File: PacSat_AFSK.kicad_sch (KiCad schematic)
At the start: 4 parts

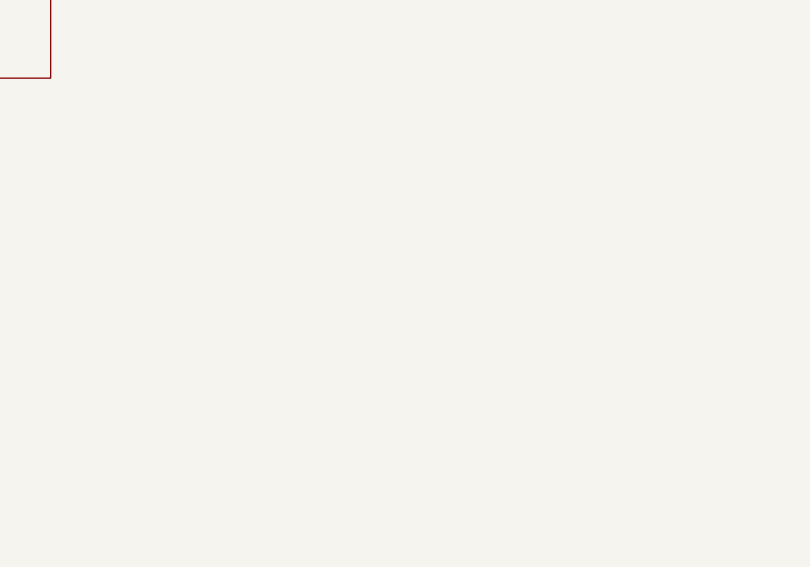
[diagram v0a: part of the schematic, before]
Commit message: Add active/standby configuration for the board
Signed-off-by: Corey Minyard <corey@minyard.net>
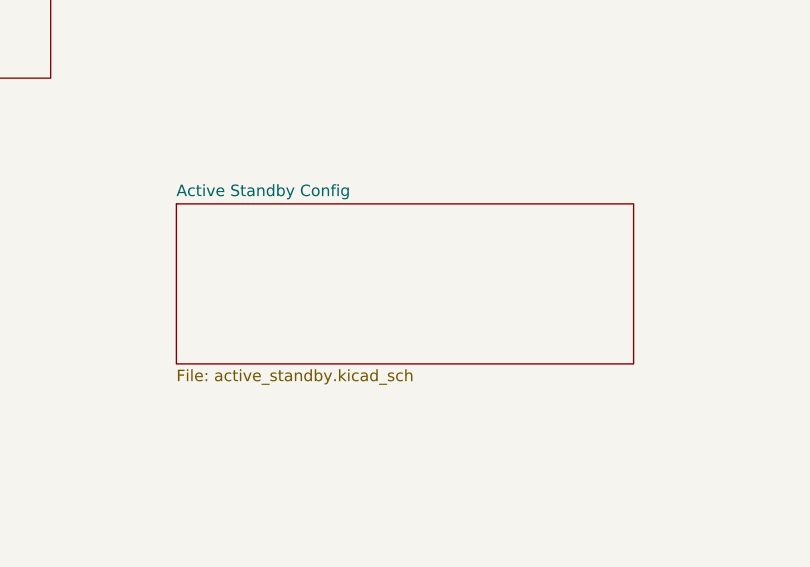
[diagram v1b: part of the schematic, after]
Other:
- added sheet Active Standby Config (active_standby.kicad_sch)
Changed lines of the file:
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@@
+	)
+	(sheet
+		(at 113.03 127)
+		(size 50.8 17.78)
+		(exclude_from_sim no)
+		(in_bom yes)
+		(on_board yes)
+		(dnp no)
+		(fields_autoplaced yes)
+		(stroke
+			(width 0.1524)
+			(type solid)
+		)
+		(fill
+			(color 0 0 0 0.0000)
+		)
+		(property "Sheetname" "Active Standby Config"
+			(at 113.03 126.2884 0)
+			(effects
+				(font
+					(size 1.27 1.27)
+				)
+				(justify left bottom)
+			)
+		)
+		(property "Sheetfile" "active_standby.kicad_sch"
+			(at 113.03 145.3646 0)
+			(effects
+				(font
+					(size 1.27 1.27)
+				)
+				(justify left top)
+			)
+		)
+		(instances
+			(project "PacSat_AFSK"
+				(path "/cc9f42d2-6985-41ac-acab-5ab7b01c5b38"
+					(page "15")
+				)
+			)
+		)
 	)
 	(sheet

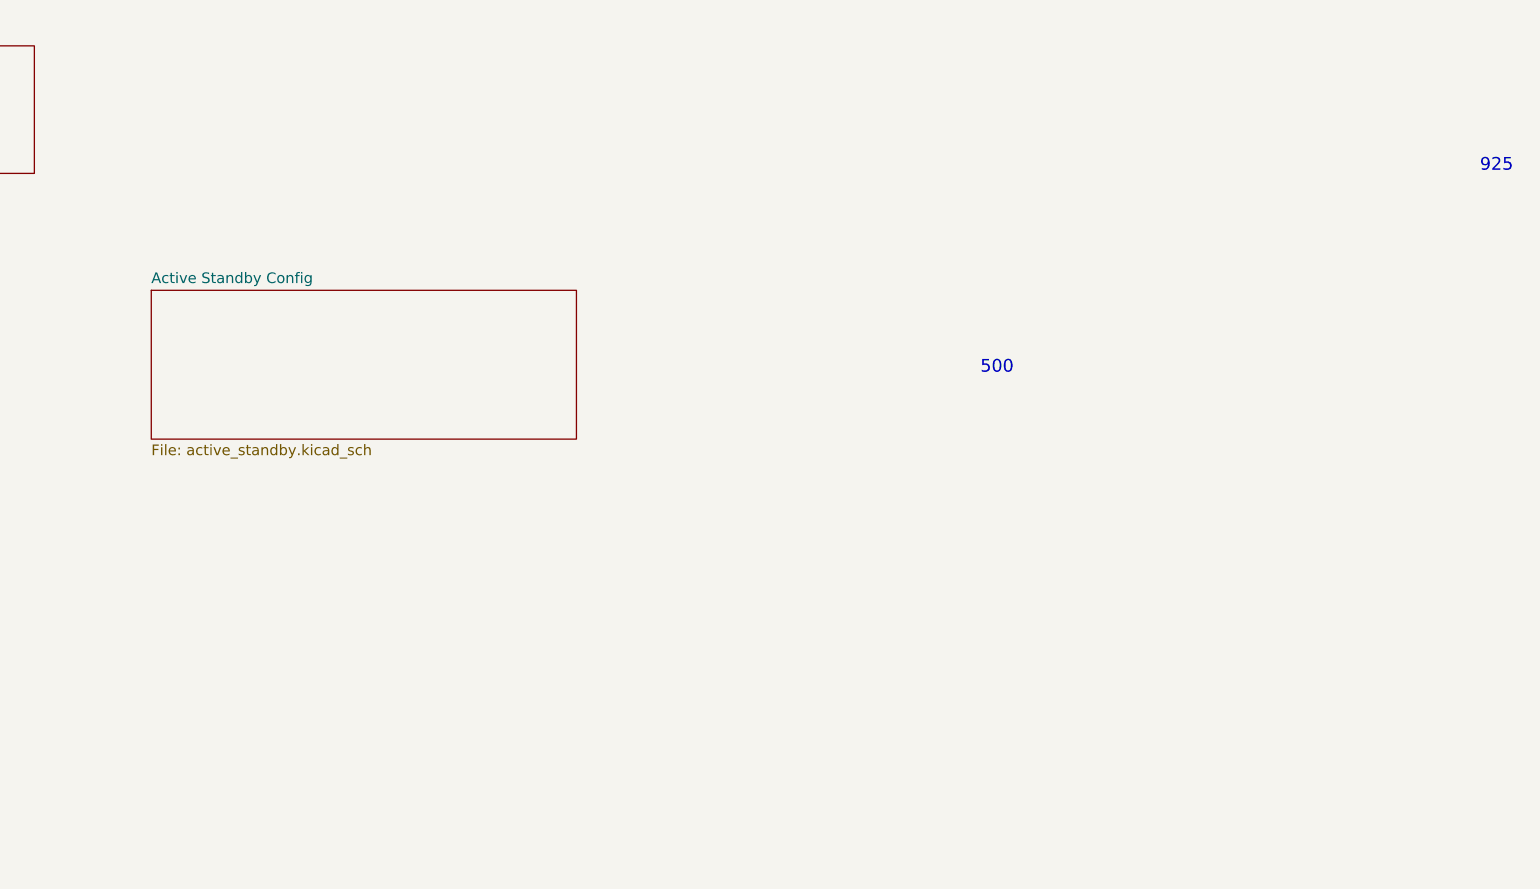
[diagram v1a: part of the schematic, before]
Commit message: Added active/standy support for TX RF and did docs
Signed-off-by: Corey Minyard <corey@minyard.net>
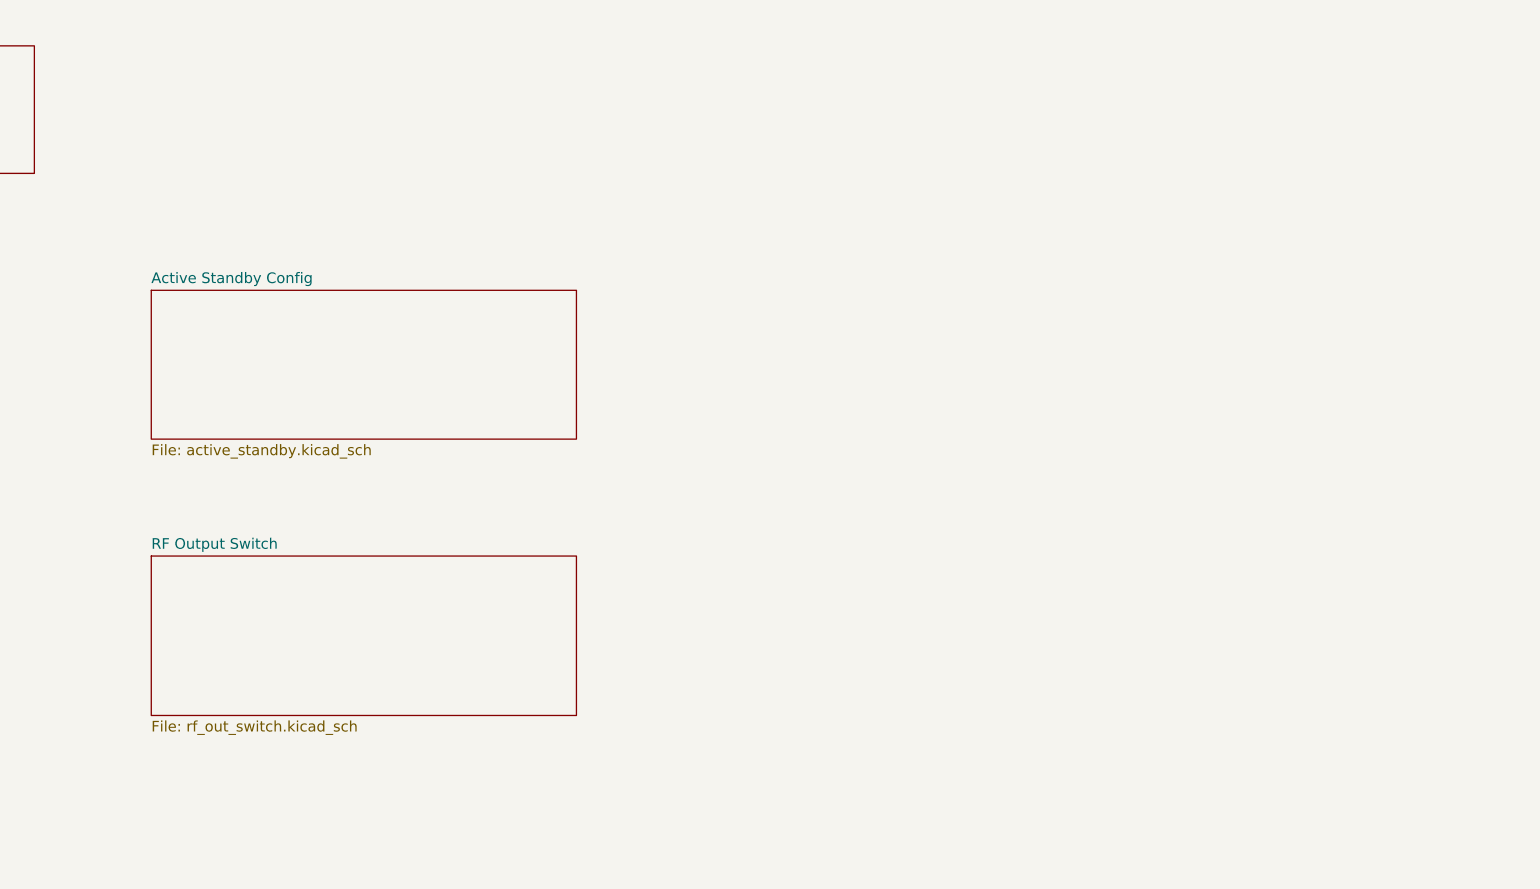
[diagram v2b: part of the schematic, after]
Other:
- added sheet RF Output Switch (rf_out_switch.kicad_sch)
- note removed: "500"
- note removed: "925"
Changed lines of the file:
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@@
 		(comment 1 "N5BRG")
-	)
-	(text "500"
-		(exclude_from_sim no)
-		(at 212.09 137.16 0)
-		(effects
-			(font
-				(size 1.524 1.524)
-			)
-			(justify left bottom)
-		)
-	)
-	(text "925"
-		(exclude_from_sim no)
-		(at 271.78 113.03 0)
-		(effects
-			(font
-				(size 1.524 1.524)
-			)
-			(justify left bottom)
-		)
 	)
 	(junction
@@
 				)
 			)
+		)
+	)
+	(sheet
+		(at 113.03 158.75)
+		(size 50.8 19.05)
+		(exclude_from_sim no)
+		(in_bom yes)
+		(on_board yes)
+		(dnp no)
+		(fields_autoplaced yes)
+		(stroke
+			(width 0.1524)
+			(type solid)
+		)
+		(fill
+			(color 0 0 0 0.0000)
+		)
+		(property "Sheetname" "RF Output Switch"
+			(at 113.03 158.0384 0)
+			(effects
+				(font
+					(size 1.27 1.27)
+				)
+				(justify left bottom)
+			)
+		)
+		(property "Sheetfile" "rf_out_switch.kicad_sch"
+			(at 113.03 178.3846 0)
+			(effects
+				(font
+					(size 1.27 1.27)
+				)
+				(justify left top)
+			)
+		)
+		(instances
+			(project "PacSat_AFSK"
+				(path "/cc9f42d2-6985-41ac-acab-5ab7b01c5b38"
+					(page "16")
+				)
+			)

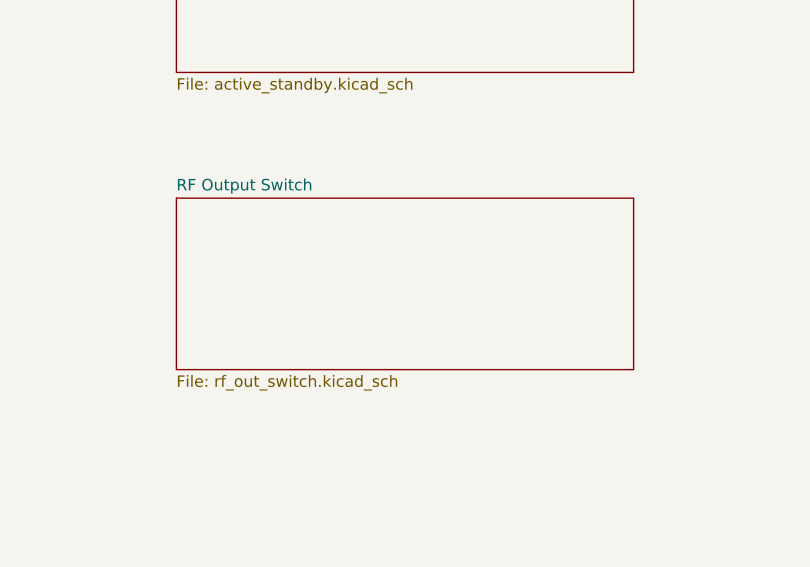
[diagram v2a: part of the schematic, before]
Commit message: Add missing sheets, move active standby to its own hierarchy
Signed-off-by: Corey Minyard <corey@minyard.net>
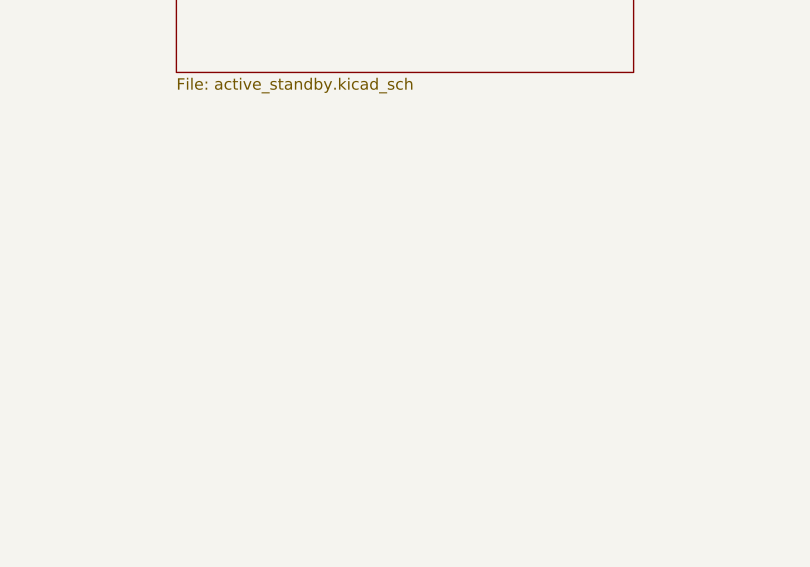
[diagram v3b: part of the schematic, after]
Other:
- removed sheet RF Output Switch
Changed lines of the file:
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@@
-	)
-	(sheet
-		(at 113.03 158.75)
-		(size 50.8 19.05)
-		(exclude_from_sim no)
-		(in_bom yes)
-		(on_board yes)
-		(dnp no)
-		(fields_autoplaced yes)
-		(stroke
-			(width 0.1524)
-			(type solid)
-		)
-		(fill
-			(color 0 0 0 0.0000)
-		)
-		(property "Sheetname" "RF Output Switch"
-			(at 113.03 158.0384 0)
-			(effects
-				(font
-					(size 1.27 1.27)
-				)
-				(justify left bottom)
-			)
-		)
-		(property "Sheetfile" "rf_out_switch.kicad_sch"
-			(at 113.03 178.3846 0)
-			(effects
-				(font
-					(size 1.27 1.27)
-				)
-				(justify left top)
-			)
-		)
-		(instances
-			(project "PacSat_AFSK"
-				(path "/cc9f42d2-6985-41ac-acab-5ab7b01c5b38"
-					(page "16")
-				)
-			)
-		)
 	)
 	(sheet

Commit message: Work on cleaning up all values for things
Signed-off-by: Corey Minyard <corey@minyard.net>
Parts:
- H2, H3, H4, H5: now left out of the parts list
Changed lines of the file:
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@@
 		(unit 1)
 		(exclude_from_sim no)
-		(in_bom yes)
+		(in_bom no)
 		(on_board yes)
 		(dnp no)
@@
 		(unit 1)
 		(exclude_from_sim no)
-		(in_bom yes)
+		(in_bom no)
 		(on_board yes)
 		(dnp no)
@@
 		(unit 1)
 		(exclude_from_sim no)
-		(in_bom yes)
+		(in_bom no)
 		(on_board yes)
 		(dnp no)
@@
 		(unit 1)
 		(exclude_from_sim no)
-		(in_bom yes)
+		(in_bom no)
 		(on_board yes)
 		(dnp no)

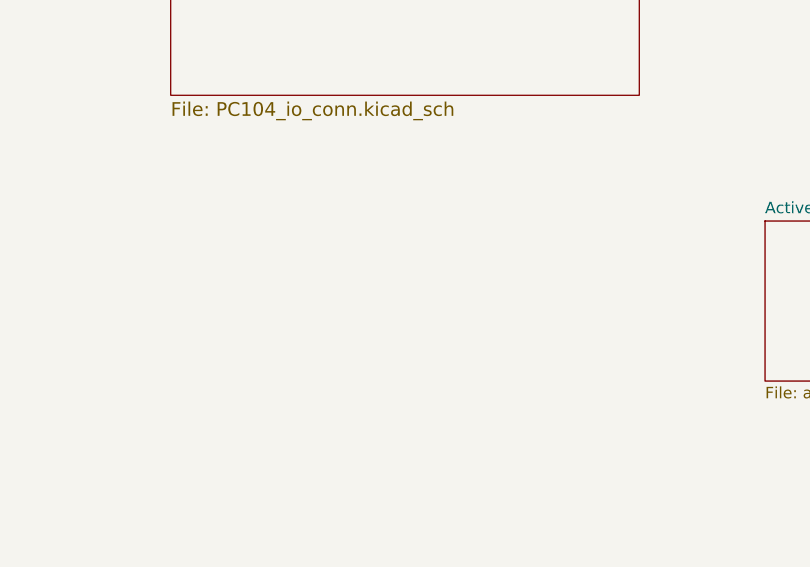
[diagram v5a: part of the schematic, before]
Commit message: Add Power System Adapter function to the board
Signed-off-by: Corey Minyard <corey@minyard.net>
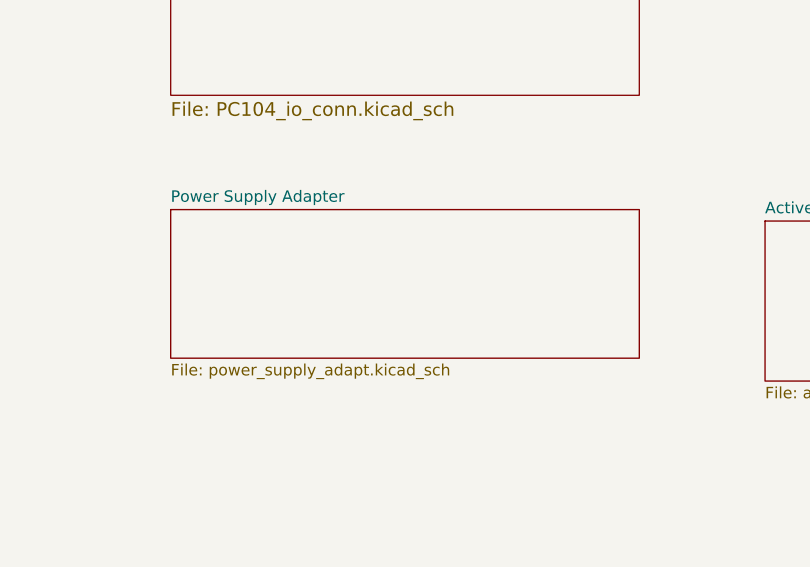
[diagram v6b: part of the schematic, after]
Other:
- added sheet Power Supply Adapter (power_supply_adapt.kicad_sch)
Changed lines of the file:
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@@
+	)
+	(sheet
+		(at 46.99 125.73)
+		(size 52.07 16.51)
+		(exclude_from_sim no)
+		(in_bom yes)
+		(on_board yes)
+		(dnp no)
+		(fields_autoplaced yes)
+		(stroke
+			(width 0.1524)
+			(type solid)
+		)
+		(fill
+			(color 0 0 0 0.0000)
+		)
+		(property "Sheetname" "Power Supply Adapter"
+			(at 46.99 125.0184 0)
+			(effects
+				(font
+					(size 1.27 1.27)
+				)
+				(justify left bottom)
+			)
+		)
+		(property "Sheetfile" "power_supply_adapt.kicad_sch"
+			(at 46.99 142.8246 0)
+			(effects
+				(font
+					(size 1.27 1.27)
+				)
+				(justify left top)
+			)
+		)
+		(instances
+			(project "PacSat_AFSK"
+				(path "/cc9f42d2-6985-41ac-acab-5ab7b01c5b38"
+					(page "18")
+				)
+			)
+		)
 	)
 	(sheet
